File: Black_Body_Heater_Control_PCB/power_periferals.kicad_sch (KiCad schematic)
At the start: 15 parts, among them Q2 SI2310-TP, U2 INA181A2IDBVR, U3 LMR51420XDDCR

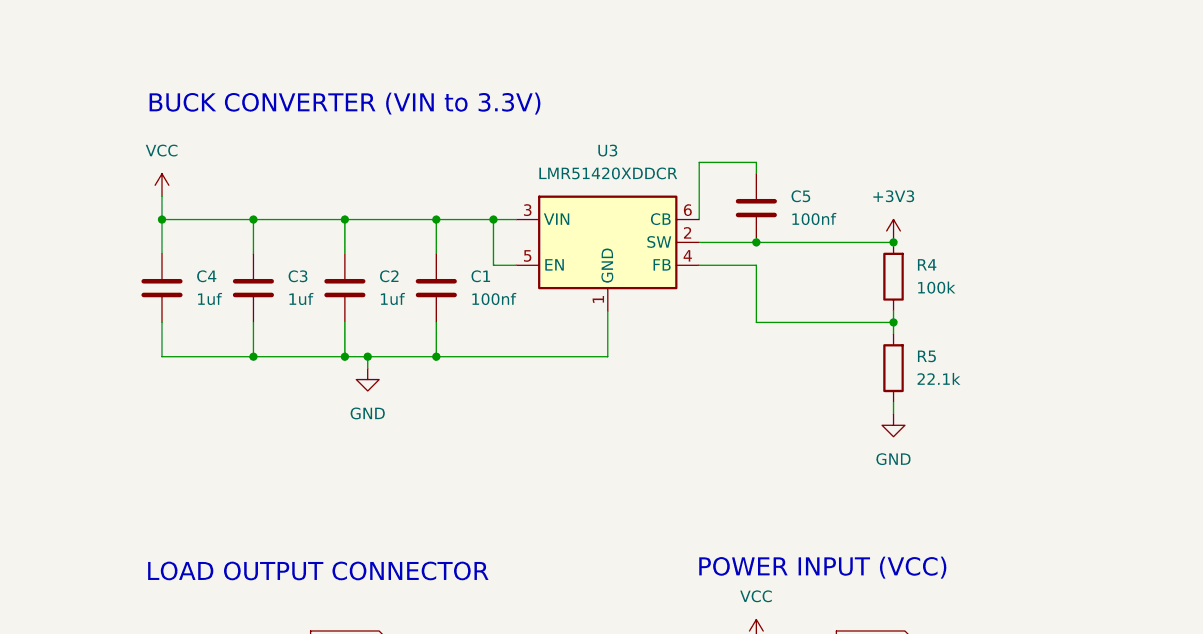
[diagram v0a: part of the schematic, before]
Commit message: Buck spice file not working, created new pcb
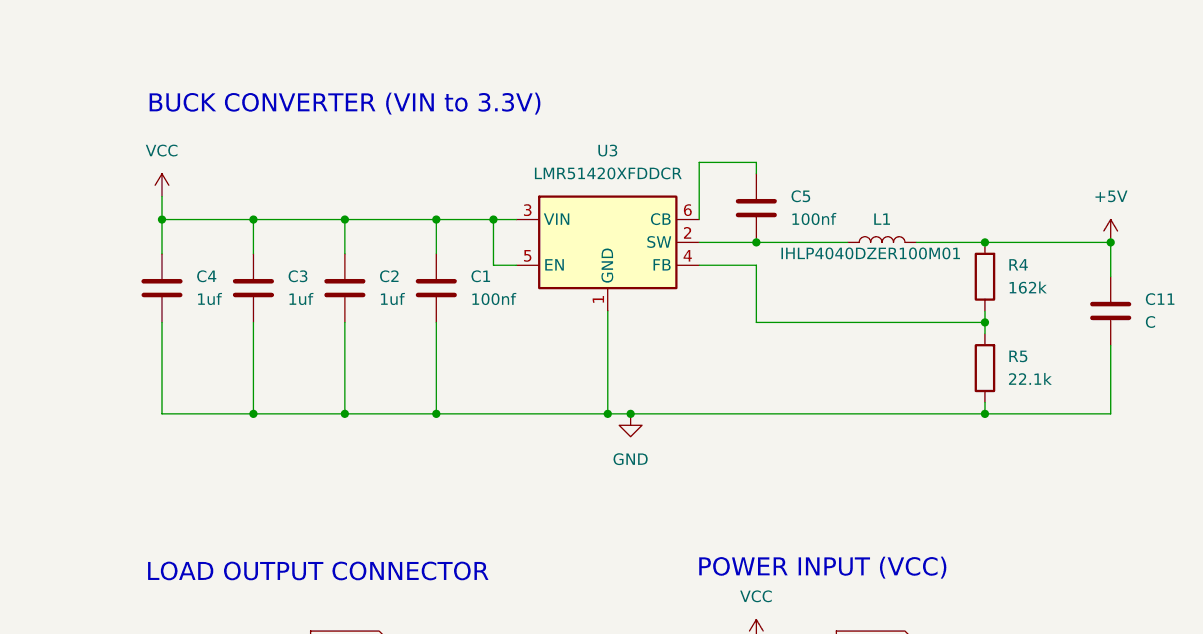
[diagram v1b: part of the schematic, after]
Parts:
- added C11: C, symbol Device:C
- added L1: IHLP4040DZER100M01, symbol Device:L
- R4: value 100k -> 162k
- U3: value LMR51420XDDCR -> LMR51420XFDDCR
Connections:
- net +3V3: no longer C5.2, R4.2, U3.2 (SW)
- net GND: now also C11.2
- new net: C5.2, L1.1, U3.2 (SW)
- new net +5V: C11.1, L1.2, R4.2
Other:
- moved on the sheet: R4, R5
